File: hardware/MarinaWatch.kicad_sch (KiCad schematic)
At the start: 34 parts, among them J201 USB_C_Receptacle_USB2.0_16P, J401 Screw_Terminal_01x04, J801 Screw_Terminal_01x02, J802 Screw_Terminal_01x03, SW101 SW_Push, SW102 SW_Push, U101 ESP32-S3-MINI-1, U301 LMV321, U302 LMV321, U303 LMV321

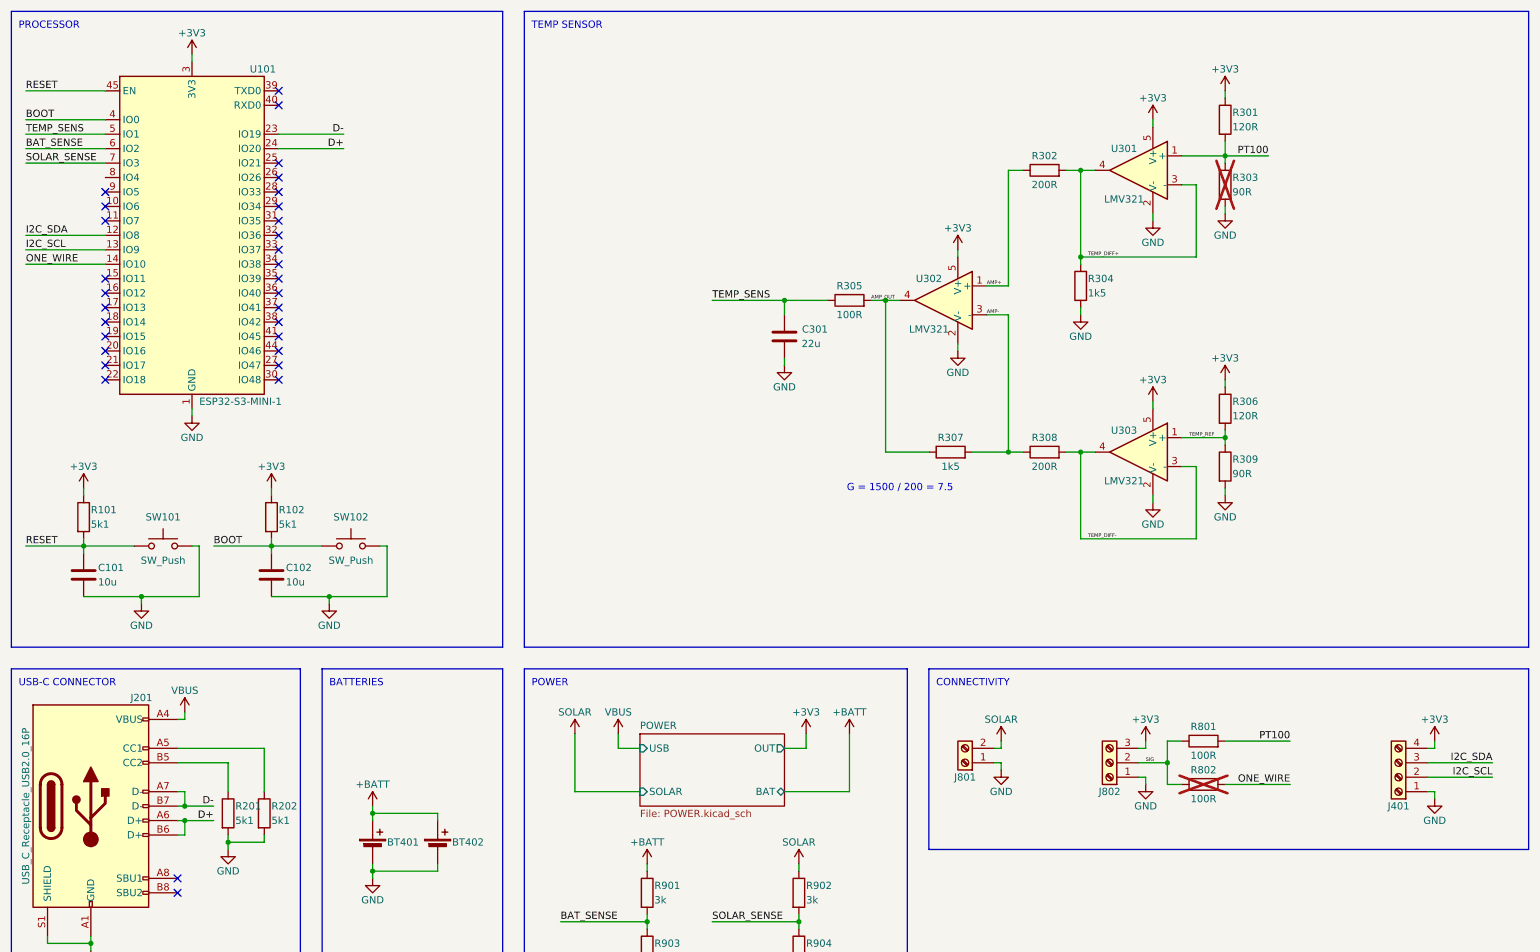
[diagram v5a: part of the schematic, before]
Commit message: Layout almost finished (missing NTCs and Buttons)
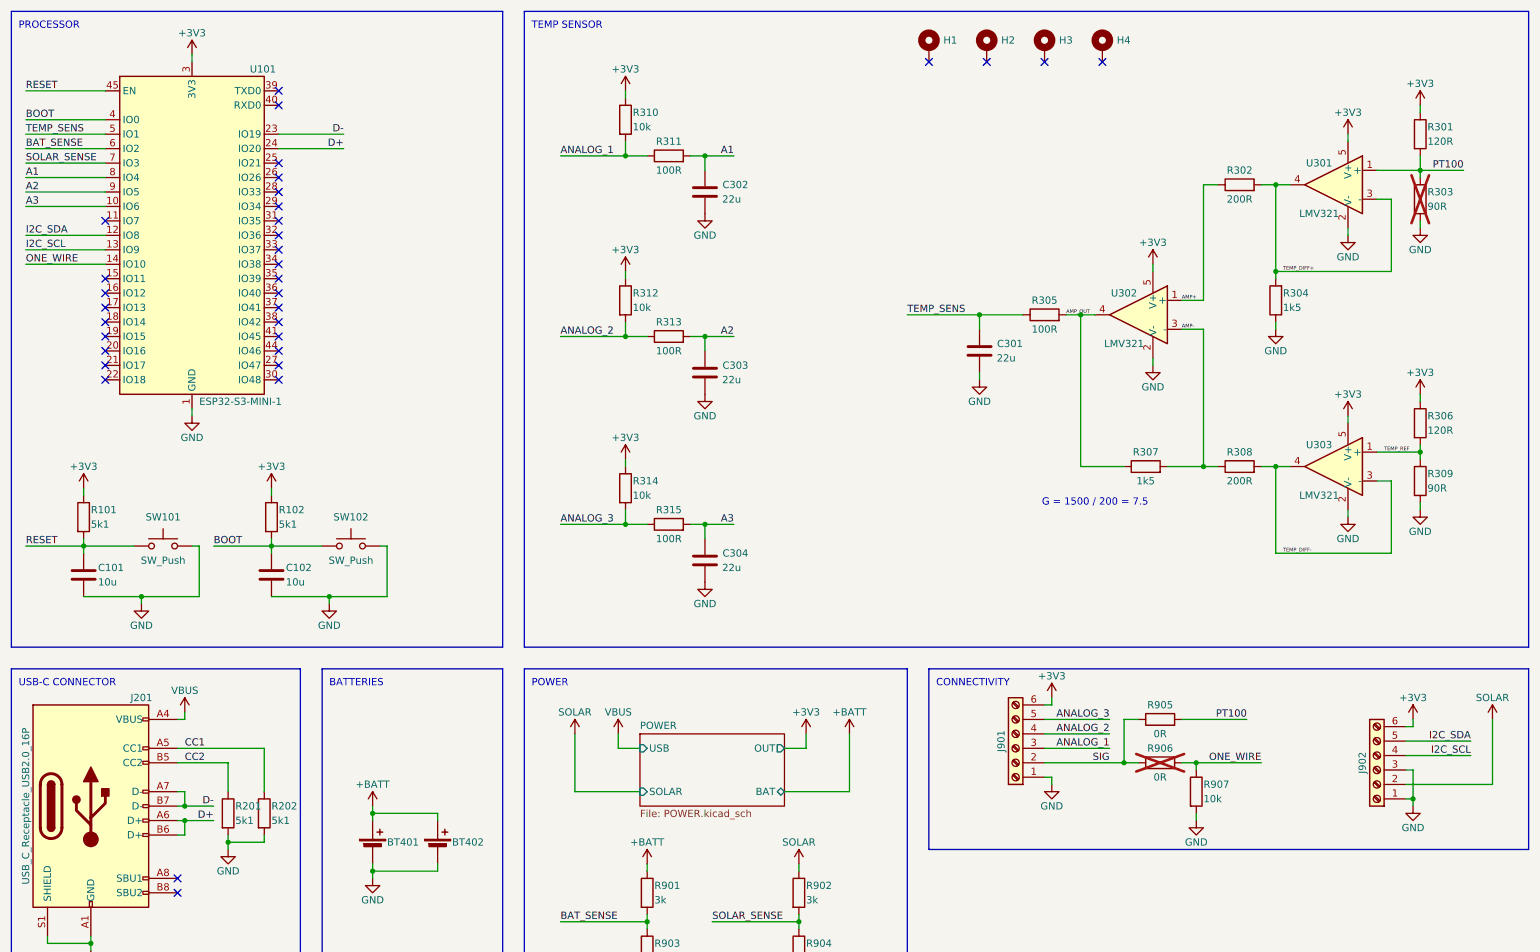
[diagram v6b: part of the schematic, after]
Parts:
- removed J401: Screw_Terminal_01x04, TerminalBlock:TerminalBlock_bornier-4_P5.08mm, symbol Connector:Screw_Terminal_01x04
- removed J801: Screw_Terminal_01x02, TerminalBlock:TerminalBlock_bornier-2_P5.08mm, symbol Connector:Screw_Terminal_01x02
- removed J802: Screw_Terminal_01x03, TerminalBlock:TerminalBlock_bornier-3_P5.08mm, symbol Connector:Screw_Terminal_01x03
- removed R801, R802: 100R, Resistor_SMD:R_0603_1608Metric_Pad0.98x0.95mm_HandSolder, symbol Device:R
- added C302, C303, C304: 22u, Capacitor_SMD:C_0603_1608Metric_Pad1.08x0.95mm_HandSolder, symbol Device:C
- added H1, H2, H3, H4: MountingHole_Pad, MountingHole:MountingHole_3.2mm_M3_DIN965_Pad, symbol Mechanical:MountingHole_Pad
- added J901, J902: Screw_Terminal_01x06, AlfredLib:THT_SCREW_01x06_P5.08mm, symbol Connector:Screw_Terminal_01x06
- added R310, R312, R314, R907: 10k, Resistor_SMD:R_0603_1608Metric_Pad0.98x0.95mm_HandSolder, symbol Device:R
- added R311, R313, R315: 100R, Resistor_SMD:R_0603_1608Metric_Pad0.98x0.95mm_HandSolder, symbol Device:R
- added R905, R906: 0R, Resistor_SMD:R_0603_1608Metric_Pad0.98x0.95mm_HandSolder, symbol Device:R
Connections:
- net +3V3: now also J901.6 (Pin_6), J902.6 (Pin_6), R310.1, R312.1, R314.1
- net GND: now also C302.2, C303.2, C304.2, J901.1 (Pin_1), J902.1 (Pin_1), J902.3 (Pin_3), R907.2
- net I2C_SCL: now also J902.4 (Pin_4)
- net I2C_SDA: now also J902.5 (Pin_5)
- net ONE_WIRE: now also R906.2, R907.1
- net PT100: now also R905.2
- net SIG: now also J901.2 (Pin_2), R905.1, R906.1
- net SOLAR: now also J902.2 (Pin_2)
- net A3: now reaches U101.10 (IO6)
- net A3: now also C304.1, R315.2
- net A1: now reaches U101.8 (IO4)
- net A1: now also C302.1, R311.2
- net A2: now reaches U101.9 (IO5)
- net A2: now also C303.1, R313.2
- net CC1: now reaches J201.A5 (CC1), R202.1
- net CC2: now reaches J201.B5 (CC2), R201.1
- new net ANALOG_1: J901.3 (Pin_3), R310.2, R311.1
- new net ANALOG_2: J901.4 (Pin_4), R312.2, R313.1
- new net ANALOG_3: J901.5 (Pin_5), R314.2, R315.1
- no-connect marks 31 -> 33
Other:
- moved on the sheet: C301, R301, R302, R303, R304, R305, R306, R307, R308, R309, U301, U302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

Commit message: First draft of HW and moved scripts
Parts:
- added C103: 10u, Capacitor_SMD:C_0603_1608Metric_Pad1.08x0.95mm_HandSolder, symbol Device:C
- added U304: ESP32-S3-WROOM-1, RF_Module:ESP32-S3-WROOM-1, symbol RF_Module:ESP32-S3-WROOM-1
- R101, R102: value 5k1 -> 10k
- R904: value 7k5 -> 3k
- SW101, SW102: footprint (none) -> AlfredLib:BUTTON_SMD_3x4mm
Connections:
- net +3V3: now also C103.1, U304.2 (3V3)
- net A1: now also U304.4 (IO4); no longer U101.8 (IO4)
- net A2: now also U304.5 (IO5); no longer U101.9 (IO5)
- net A3: now also U304.6 (IO6); no longer U101.10 (IO6)
- net BAT_SENSE: now also U304.38 (IO2); no longer U101.6 (IO2)
- net BOOT: now also U304.27 (IO0); no longer U101.4 (IO0)
- net D+: now also U304.14 (IO20); no longer U101.24 (IO20)
- net D-: now also U304.13 (IO19); no longer U101.23 (IO19)
- net GND: now also C103.2, U304.1 (GND), U304.40 (GND), U304.41 (GND)
- net I2C_SCL: now also U304.17 (IO9); no longer U101.13 (IO9)
- net I2C_SDA: now also U304.12 (IO8); no longer U101.12 (IO8)
- net ONE_WIRE: now also U304.18 (IO10); no longer U101.14 (IO10)
- net RESET: now also U304.3 (EN); no longer U101.45 (EN)
- net SOLAR_SENSE: now also U304.15 (IO3); no longer U101.7 (IO3)
- net TEMP_SENS: now also U304.39 (IO1); no longer U101.5 (IO1)
- no-connect marks 33 -> 57
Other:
- note added: "4.2V -> 3.0V"
- note added: "6.0V -> 3.0V"
- moved on the sheet: BT401, BT402, R202

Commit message: Recond draft of HW
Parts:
- removed U101: ESP32-S3-MINI-1, RF_Module:ESP32-S2-MINI-1, symbol RF_Module:ESP32-S3-MINI-1
- added R316: 0R, Resistor_SMD:R_0603_1608Metric_Pad0.98x0.95mm_HandSolder, symbol Device:R
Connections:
- net A1: now also U304.6 (IO6); no longer U304.4 (IO4)
- net A3: now also U304.4 (IO4); no longer U304.6 (IO6)
- net BOOT: now also R316.2
- net RESET: now also R316.1
- no-connect marks 57 -> 30
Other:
- moved on the sheet: C101, C102, R101, R102, SW101, SW102, U304
